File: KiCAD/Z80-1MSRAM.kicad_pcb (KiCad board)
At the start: 2 copper layers, 99.1 x 74.9 mm, 31 parts, among them J1 SBC8080 BUS, J2 I/O ADDR SEL, Q1 2SC1815, U1 74HC02, U2 74HC74, U3 74HC139, U4 74HC04, U5 74HC00, U6 628128, U7 28C256

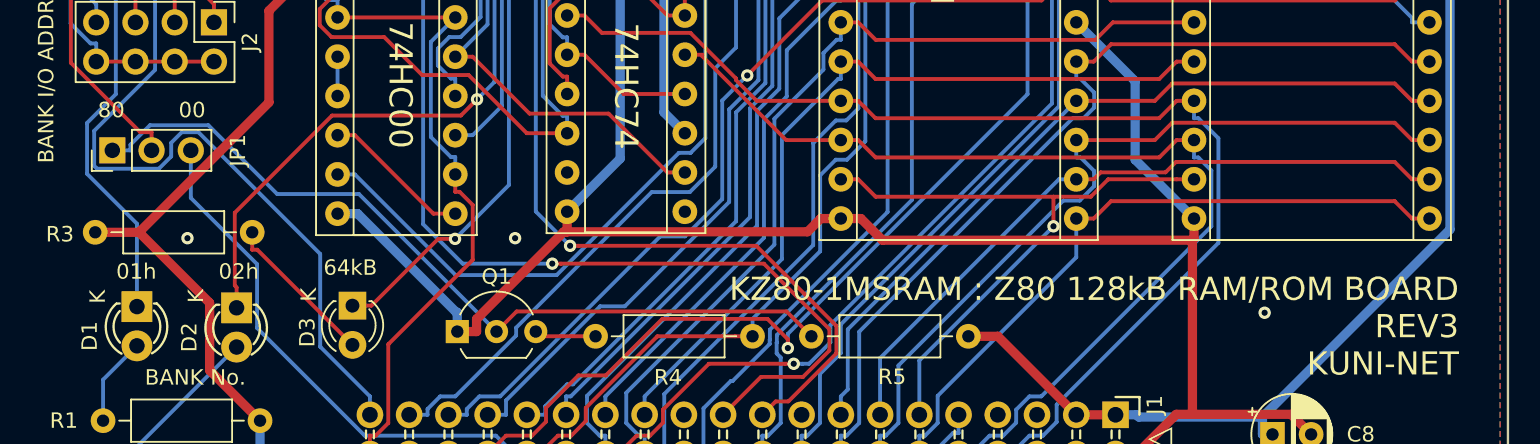
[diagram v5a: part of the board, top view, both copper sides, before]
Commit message: REV3からREV2.1へ改名 回路図 & 製造データ出力
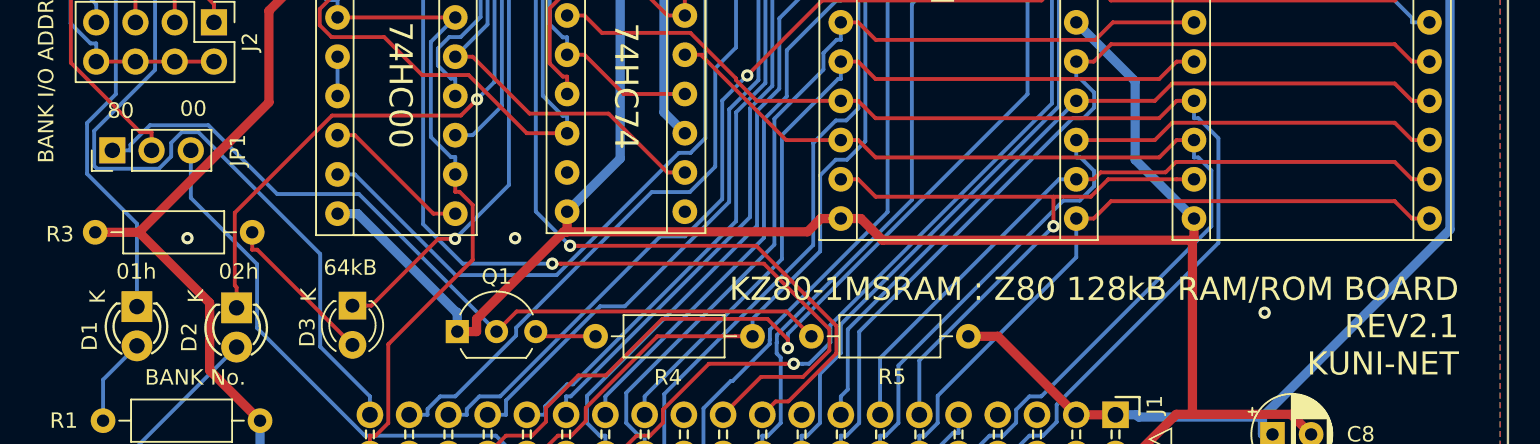
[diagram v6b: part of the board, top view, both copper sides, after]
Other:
- board text added: "KZ80-1MSRAM : Z80 128kB RAM/ROM BOARD REV2.1 KUNI-NET"
- board text removed: "KZ80-1MSRAM : Z80 128kB RAM/ROM BOARD REV3 KUNI-NET"
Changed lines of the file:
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@@
     (pad 1 np_thru_hole circle (at 0 0) (size 3.2 3.2) (drill 3.2) (layers *.Cu *.Mask))
   )
-  (gr_text 80 (at 110.25632 105.37444) (layer F.SilkS)
+  (gr_text 80 (at 110.871 105.41) (layer F.SilkS)
     (effects (font (size 1 1) (thickness 0.15)))
   )
@@
     (effects (font (size 1 1) (thickness 0.15)))
   )
-  (gr_text 00 (at 115.48872 105.37444) (layer F.SilkS)
+  (gr_text 00 (at 115.57 105.283) (layer F.SilkS)
     (effects (font (size 1 1) (thickness 0.15)))
   )
@@
     (effects (font (size 1 1) (thickness 0.15)))
   )
-  (gr_text "KZ80-1MSRAM : Z80 128kB RAM/ROM BOARD\nREV3\nKUNI-NET" (at 197.485 119.38) (layer F.SilkS)
+  (gr_text "KZ80-1MSRAM : Z80 128kB RAM/ROM BOARD\nREV2.1\nKUNI-NET" (at 197.485 119.38) (layer F.SilkS)
     (effects (font (size 1.5 1.5) (thickness 0.3)) (justify right))
   )

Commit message: REV3 回路図、プリントパターン、ガーバーデータ
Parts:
- added C9: 22p, Capacitor_THT:C_Disc_D3.0mm_W1.6mm_P2.50mm, F.Cu at (129.9, 118.1)
- added JP2: 16k/32k, Connector_PinHeader_2.54mm:PinHeader_1x03_P2.54mm_Vertical, F.Cu at (105.4, 85.0)
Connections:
- U3 pad 14: /A14 -> Net-(JP2-Pad2)
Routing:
- net GND: track 285.2 -> 328.9 mm, vias 6 -> 0
- net /A13: track 98.1 -> 133.0 mm
- net /A6: track 122.3 -> 151.5 mm
- net /A10: track 80.0 -> 100.7 mm, vias 1 -> 0
- net Net-(D3-Pad1): track 46.9 -> 62.7 mm, vias 1 -> 0
- net /D0: track 83.3 -> 67.6 mm, vias 0 -> 1
- net Net-(JP2-Pad2): track 0.00 -> 14.5 mm
- net Net-(D1-Pad1): track 55.9 -> 68.1 mm, vias 1 -> 0
- net Net-(C9-Pad1): track 4.00 -> 13.9 mm
- net ~IOWR: track 69.5 -> 79.2 mm
- net Net-(J2-Pad2): track 71.6 -> 62.6 mm
- net Net-(U2-Pad13): track 47.8 -> 39.1 mm, vias 1 -> 0
- net Net-(U1-Pad13): track 58.4 -> 66.6 mm
- net /DA1: track 61.9 -> 69.2 mm
- net Net-(JP1-Pad1): track 52.9 -> 60.1 mm
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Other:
- board text added: "16k"
- board text added: "32k"
- board text added: "KZ80-1MSRAM : Z80 128kB RAM/ROM BOARD REV3 KUNI-NET"
- board text removed: "KZ80-1MSRAM : Z80 128kB RAM/ROM BOARD REV2.1 KUNI-NET"

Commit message: REV4基板 ガーバーデータ出力
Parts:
- added J3: MSX SLOT, Connector_PinHeader_2.54mm:PinHeader_1x05_P2.54mm_Vertical, F.Cu at (159.0, 62.5)
- added JP3: RAMCSJP, Connector_PinHeader_2.54mm:PinHeader_1x03_P2.54mm_Vertical, F.Cu at (180.5, 62.5)
- added JP4: ROMCSJP, Connector_PinHeader_2.54mm:PinHeader_1x03_P2.54mm_Vertical, F.Cu at (180.5, 66.0)
- moved MH1 3.87 mm to (105.5, 64.5)
- moved MH3 3.87 mm to (105.5, 130.5)
- moved MH2 3.82 mm to (194.5, 64.5)
- moved MH4 3.80 mm to (194.5, 130.5)
- moved C1 3.50 mm to (147.9, 66.0)
- moved C2 3.50 mm to (147.8, 89.8)
- moved C3 3.50 mm to (117.4, 68.5)
- moved C4 3.50 mm to (133.1, 65.8)
- moved C5 3.50 mm to (133.0, 89.9)
- moved C6 3.50 mm to (172.7, 67.6)
- moved C7 3.50 mm to (195.5, 72.7)
- moved C8 3.50 mm to (185.4, 122.9)
- moved C9 3.50 mm to (129.9, 114.6)
- moved D1 3.50 mm to (111.9, 114.6)
- moved D2 3.50 mm to (118.4, 114.7)
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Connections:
- J1 pad 17: Net-(J1-Pad17) -> (no net)
- J1 pad 22: Net-(J1-Pad22) -> (no net)
- J1 pad 23: Net-(J1-Pad23) -> (no net)
- J1 pad 24: Net-(J1-Pad24) -> (no net)
- J1 pad 5: Net-(J1-Pad5) -> (no net)
- J1 pad 6: Net-(J1-Pad6) -> (no net)
- J1 pad 7: Net-(J1-Pad7) -> (no net)
- J1 pad 8: Net-(J1-Pad8) -> (no net)
- U1 pad 13: Net-(U1-Pad13) -> Net-(JP3-Pad3)
- U2 pad 6: Net-(U2-Pad6) -> (no net)
- U2 pad 8: Net-(U2-Pad8) -> (no net)
- U3 pad 10: Net-(U3-Pad10) -> (no net)
- U3 pad 11: Net-(U3-Pad11) -> (no net)
- U3 pad 9: Net-(U3-Pad9) -> (no net)
- U6 pad 30: Net-(U1-Pad13) -> Net-(JP3-Pad2)
- U7 pad 20: Net-(U1-Pad13) -> Net-(JP4-Pad2)
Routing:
- net Net-(U1-Pad13): track 66.6 -> 0.00 mm
- net Net-(JP3-Pad3): track 0.00 -> 47.0 mm
- net Net-(JP4-Pad2): track 0.00 -> 35.6 mm
- net GND: track 328.9 -> 297.5 mm
- net /A11: track 87.9 -> 114.4 mm, vias 1 -> 0
- net /A6: track 151.5 -> 127.1 mm
- net Net-(J3-Pad1): track 0.00 -> 23.2 mm
- net /A10: track 100.7 -> 80.7 mm, vias 0 -> 1
- net Net-(JP3-Pad2): track 0.00 -> 18.3 mm
- net VCC: track 283.6 -> 301.2 mm
- net Net-(D1-Pad1): track 68.1 -> 51.5 mm
- net Net-(J2-Pad2): track 62.6 -> 47.0 mm, vias 0 -> 1
- net Net-(D3-Pad1): track 62.7 -> 47.1 mm, vias 0 -> 1
- net Net-(J3-Pad4): track 0.00 -> 15.1 mm
- net ~IOWR: track 79.2 -> 65.2 mm
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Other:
- board size 99.1 x 74.9 mm -> 100 x 75 mm
- board text added: "KZ80"
- board text added: "KZ80-1MSRAM : Z80 128kB RAM/ROM BOARD REV4 KUNI-NET 2021"
- board text added: "MSX"
- board text added: "MSX MEM SLOT"
- board text removed: "KZ80-1MSRAM : Z80 128kB RAM/ROM BOARD REV3 KUNI-NET"
